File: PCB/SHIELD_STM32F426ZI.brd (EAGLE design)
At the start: 92.4 x 119.5 mm, 16 parts, among them IC1 AS4C16M16SA-6TCN, J1 104239-1430

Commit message: PCB wurde mit kurzer Leitung korrigiert
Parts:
- moved R3 31.7 mm to (65.9, 36.3), turned to 90 degrees
- moved R27 29.6 mm to (62.4, 36.2), turned to 270 degrees
- moved R29 26.7 mm to (64.4, 36.3), turned to 270 degrees
- moved R26 26.0 mm to (59.3, 36.3), turned to 270 degrees
- moved R28 25.8 mm to (57.7, 36.4), turned to 270 degrees
- moved R31 25.5 mm to (56.1, 36.3), turned to 270 degrees
- moved R30 24.8 mm to (60.8, 36.3), turned to 270 degrees
- moved JP3 22.6 mm to (31.6, 82.3), turned to 270 degrees
- moved R1 21.3 mm to (70.0, 36.3)
- moved JP2 20.8 mm to (53.1, 40.3)
- moved C18 19.8 mm to (67.3, 36.3), turned to 270 degrees
- moved R2 17.6 mm to (68.9, 36.4)
- moved J1 11.7 mm to (42.5, 20.3)
- moved JP1 11.2 mm to (39.9, 47.6)
- moved IC1 5.61 mm to (44.1, 79.2)
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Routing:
- net FMC_D0: track 166.7 -> 44.4 mm, vias 0 -> 2
- net FMC_D1: track 160.7 -> 49.7 mm, vias 0 -> 2
- net FMC_SDNE0: track 201.3 -> 91.6 mm, vias 2 -> 1
- net FMC_D4: track 162.8 -> 53.6 mm, vias 2 -> 1
- net FMC_D5: track 163.0 -> 56.3 mm, vias 2 -> 1
- net FMC_D13: track 163.8 -> 65.4 mm, vias 2 -> 0
- net FMC_SDCKE0: track 147.3 -> 53.5 mm, vias 2 -> 3
- net FMC_A5: track 139.1 -> 53.8 mm, vias 2 -> 1
- net FMC_SDNWE: track 122.8 -> 40.0 mm, vias 2 -> 1
- net FMC_A4: track 135.8 -> 53.3 mm, vias 2 -> 0
- net FMC_D6: track 140.1 -> 65.3 mm, vias 2 -> 1
- net FMC_A8: track 108.1 -> 34.1 mm, vias 2 -> 0
- net GND: track 7.15 -> 77.8 mm, vias 5 -> 8
- net FMC_D8: track 98.1 -> 28.5 mm
- net FMC_D7: track 121.8 -> 54.9 mm, vias 2 -> 1
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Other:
- board size 92.4 x 119.5 mm -> 89.8 x 119.7 mm

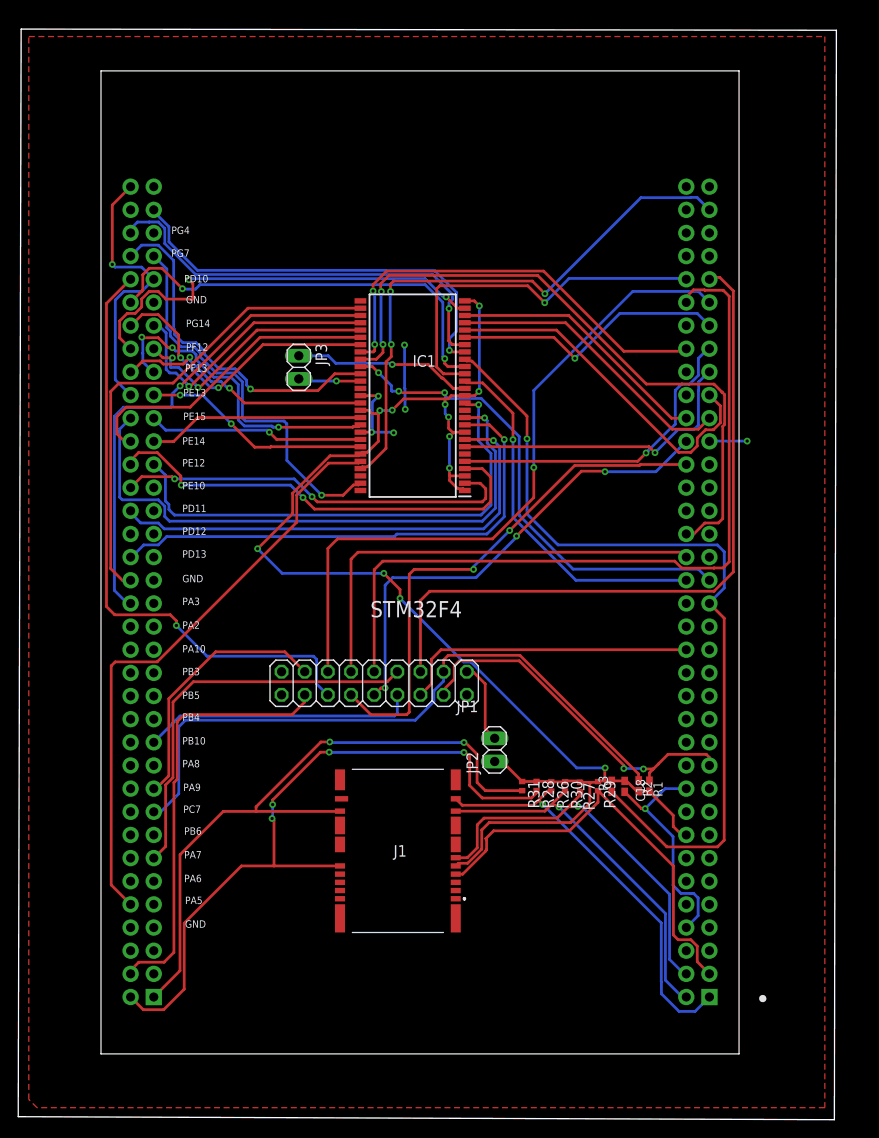
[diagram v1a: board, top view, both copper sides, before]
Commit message: Namen der Elementen und Pin hinzufügen
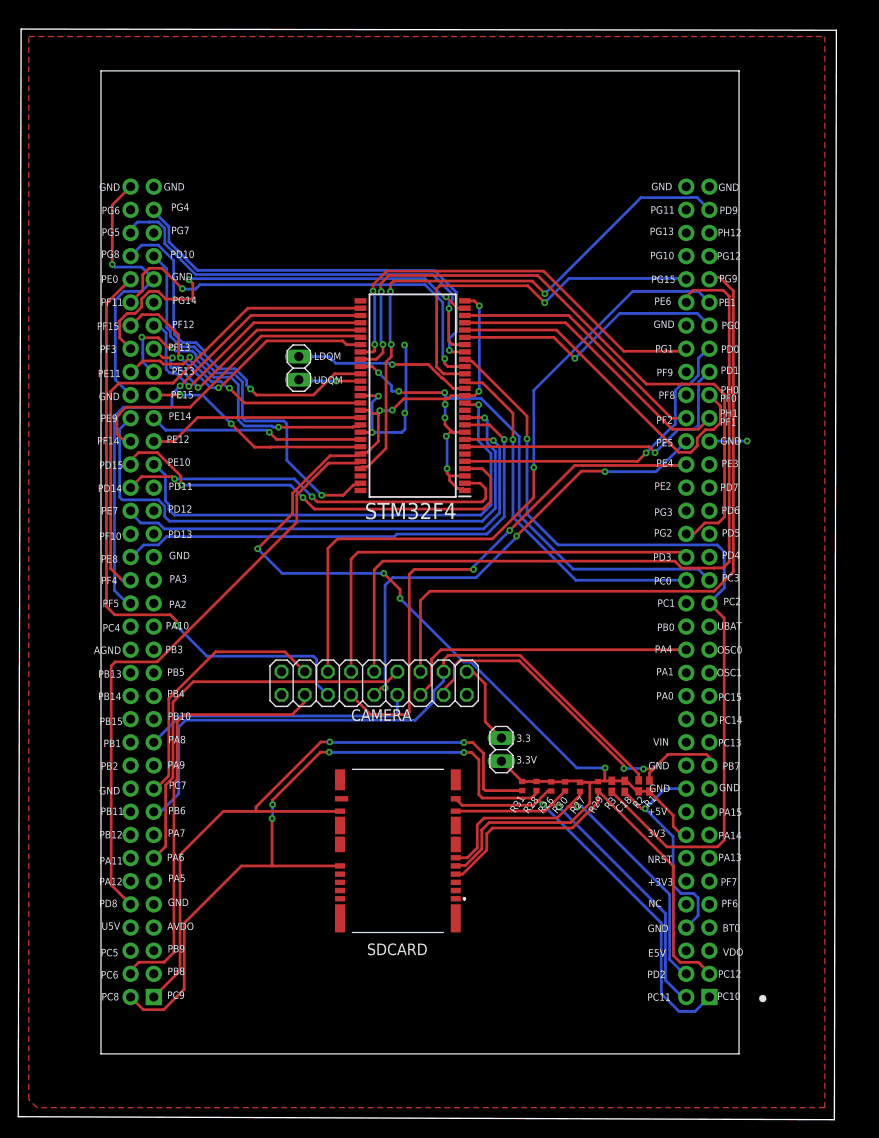
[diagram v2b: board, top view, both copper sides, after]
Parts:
- moved JP2 0.74 mm to (53.8, 40.3)
- moved JP3 0.09 mm to (31.6, 82.2)
- renumbered J1 to SDCARD, JP1 to CAMERA
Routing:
- net GND: track 77.8 -> 80.9 mm, vias 8 -> 7
- net SDIO_CK: track 47.0 -> 47.5 mm
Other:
- board text added: "+3V3"
- board text added: "+5V"
- board text added: "3.3"
- board text added: "3.3V"
- board text added: "3V3"
- board text added: "AGND"
- board text added: "AVDO"
- board text added: "BT0"
- board text added: "E5V"
- board text added: "LDQM"
- board text added: "NC"
- board text added: "NRST"
- board text added: "OSC0"
- board text added: "OSC1"
- board text added: "PA0"
- board text added: "PA1"
- board text added: "PA11"
- board text added: "PA12"
- board text added: "PA13"
- board text added: "PA14"
- board text added: "PA15"
- board text added: "PA4"
- board text added: "PB0"
- board text added: "PB1"
- board text added: "PB11"
- board text added: "PB12"
- board text added: "PB13"
- board text added: "PB14"
- board text added: "PB15"
- board text added: "PB2"
- board text added: "PB7"
- board text added: "PB8"
- board text added: "PB9"
- board text added: "PC0"
- board text added: "PC1"
- board text added: "PC10"
- board text added: "PC11"
- board text added: "PC12"
- board text added: "PC13"
- board text added: "PC14"
- board text added: "PC15"
- board text added: "PC2"
- board text added: "PC3"
- board text added: "PC4"
- board text added: "PC5"
- board text added: "PC6"
- board text added: "PC8"
- board text added: "PC9"
- board text added: "PD0"
- board text added: "PD1"
- board text added: "PD14"
- board text added: "PD15"
- board text added: "PD2"
- board text added: "PD3"
- board text added: "PD4"
- board text added: "PD5"
- board text added: "PD6"
- board text added: "PD7"
- board text added: "PD8"
- board text added: "PD9"
- board text added: "PE0"
- board text added: "PE1"
- board text added: "PE11"
- board text added: "PE2"
- board text added: "PE3"
- board text added: "PE4"
- board text added: "PE5"
- board text added: "PE6"
- board text added: "PE7"
- board text added: "PE8"
- board text added: "PE9"
- board text added: "PF0"
- board text added: "PF1"
- board text added: "PF10"
- board text added: "PF11"
- board text added: "PF14"
- board text added: "PF15"
- board text added: "PF2"
- board text added: "PF3"
- board text added: "PF4"
- board text added: "PF5"
- board text added: "PF6"
- board text added: "PF7"
- board text added: "PF8"
- board text added: "PF9"
- board text added: "PG0"
- board text added: "PG1"
- board text added: "PG10"
- board text added: "PG11"
- board text added: "PG12"
- board text added: "PG13"
- board text added: "PG15"
- board text added: "PG2"
- board text added: "PG3"
- board text added: "PG5"
- board text added: "PG6"
- board text added: "PG8"
- board text added: "PG9"
- board text added: "PH0"
- board text added: "PH1"
- board text added: "PH12"
- board text added: "U5V"
- board text added: "UBAT"
- board text added: "UDQM"
- board text added: "VDO"
- board text added: "VIN"

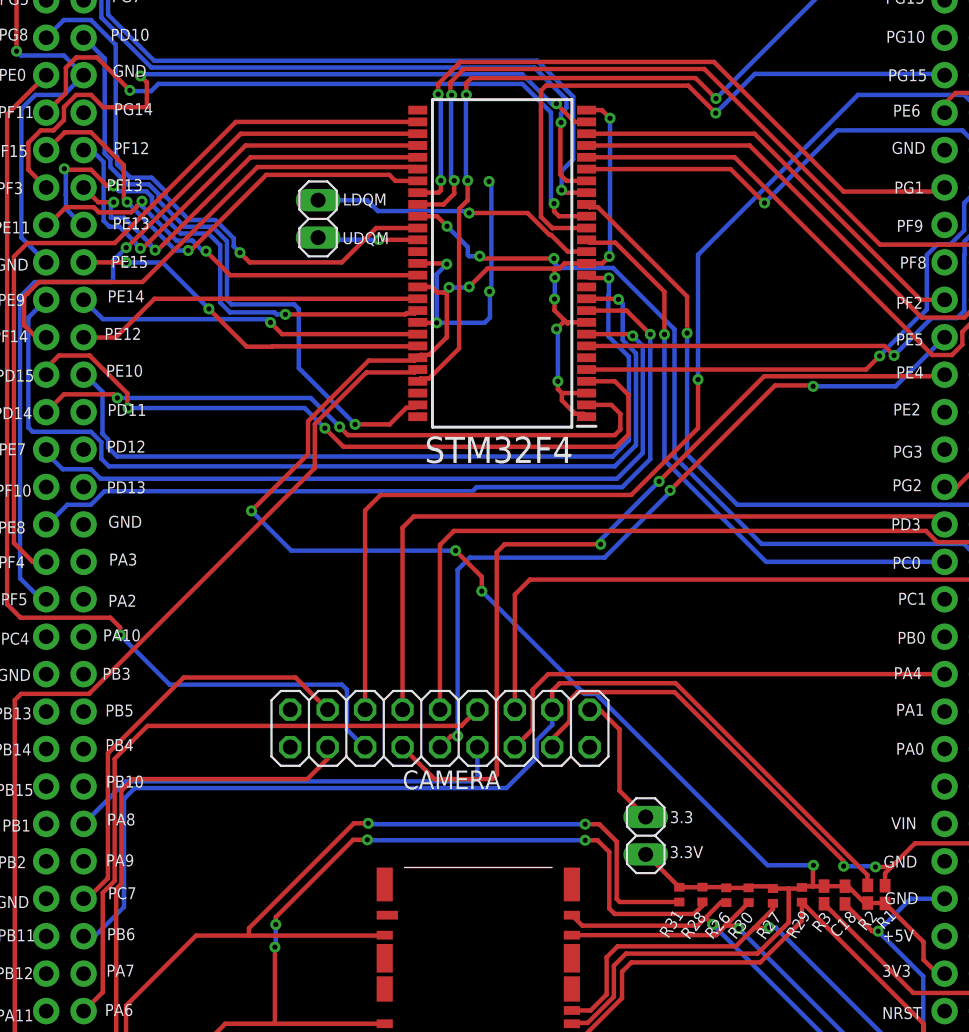
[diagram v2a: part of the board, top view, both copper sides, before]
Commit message: Namen der DCMI-Pins hinzufügen und Position des Kondensators korrigieren
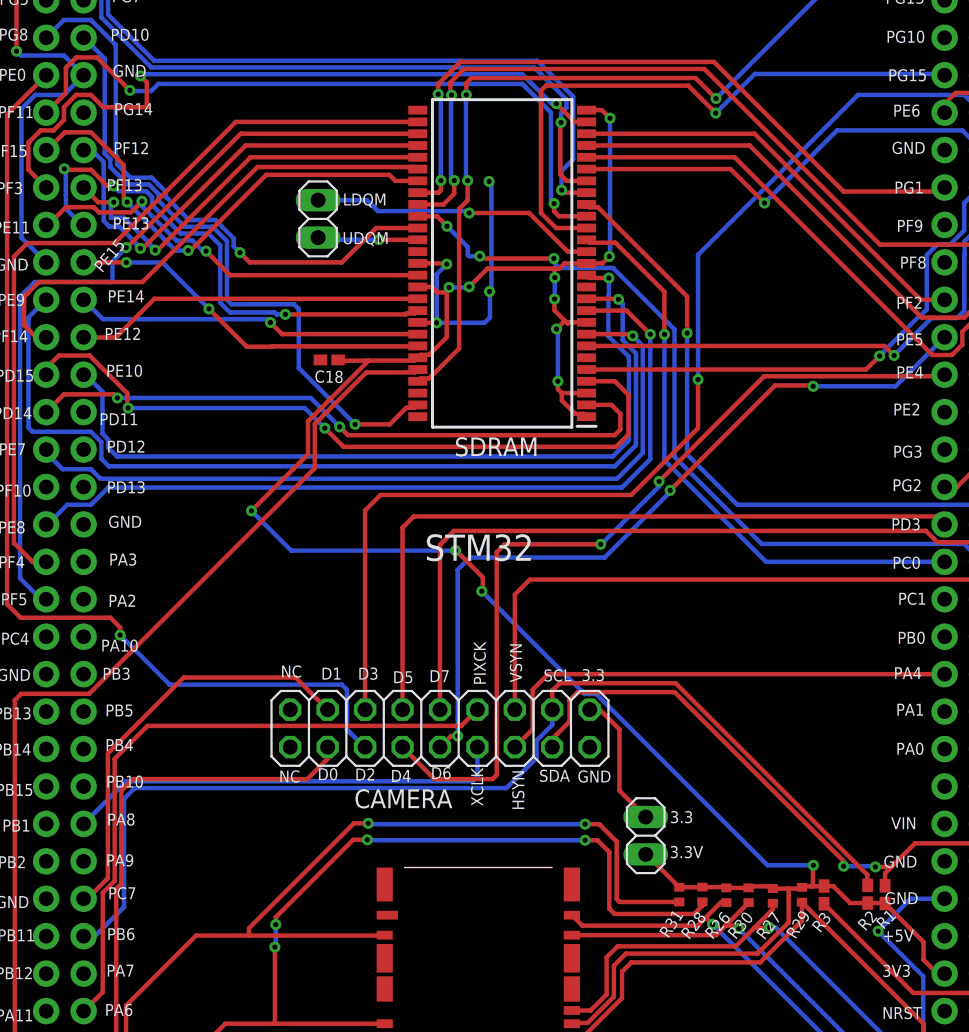
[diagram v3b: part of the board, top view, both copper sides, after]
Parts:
- moved C18 50.4 mm to (32.3, 72.6), turned to 180 degrees
- renumbered IC1 to SDRAM, STM32F4 to STM32
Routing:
- net GND: track 80.9 -> 77.9 mm
- net 3.3V: track 159.2 -> 161.4 mm
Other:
- board text added: "D0"
- board text added: "D1"
- board text added: "D2"
- board text added: "D3"
- board text added: "D4"
- board text added: "D5"
- board text added: "D6"
- board text added: "D7"
- board text added: "HSYN"
- board text added: "PIXCK"
- board text added: "SCL"
- board text added: "SDA"
- board text added: "SDRAM"
- board text added: "VSYN"
- board text added: "XCLK"

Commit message: new update
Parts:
- CAMERA, JP2, JP3: value (none) -> 0
- moved R2 1.25 mm to (67.6, 36.5)
- moved R1 1.13 mm to (68.9, 36.4)
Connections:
- new net PWDN: CAMERA.18, STM32.CN12_29
- net CARD_DET: now also STM32.CN12_11
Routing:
- net CARD_DET: track 0.00 -> 25.3 mm, vias 0 -> 1
- net PWDN: track 0.00 -> 15.0 mm
- net GND: track 77.9 -> 76.7 mm
- net I2C1_SDA: track 40.1 -> 41.2 mm
- net 3.3V: track 161.4 -> 160.8 mm
- net I2C1_SCL: track 72.7 -> 72.2 mm
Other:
- board text added: "AD-HOC"
- board text added: "PA5/CARD_DET"
- board text removed: "PA5"

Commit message: new layout update
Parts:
- renumbered C18 to C1, R26 to R7, R27 to R5, R28 to R8, R29 to R4, R30 to R6, R31 to R9
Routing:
- net FMC_D14: track 62.8 -> 66.6 mm
- net SDIO_D1: track 73.5 -> 75.9 mm
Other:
- board size 89.8 x 119.7 mm -> 83 x 120.2 mm

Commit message: add mosfet and fix GPIOs for sdram and sdcard
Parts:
- removed JP2, JP3: 0, pinhead:1X02
- added Q1: FDN304P, FDN304P:SOT95P237X112-3N
- moved R2 2.20 mm to (69.8, 36.3)
- moved R1 0.99 mm to (67.9, 36.3)
- moved R3 0.49 mm to (66.4, 36.3), turned to 270 degrees
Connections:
- removed net FMC_SDCKE0: SDRAM.37, STM32.CN11_37
- removed net FMC_SDNE0: R3.1, SDRAM.19, STM32.CN11_35
- removed net I2C1_SCL: CAMERA.3, R2.1, STM32.CN12_17
- removed net I2C1_SDA: CAMERA.4, R1.1, STM32.CN11_21
- new net FMC_SDCKE1: SDRAM.37, STM32.CN12_29
- new net FMC_SDNE1: R3.1, SDRAM.19, STM32.CN12_17
- new net GATE: Q1.1, STM32.CN11_35
- new net I2C2_SCL: CAMERA.3, R2.1, STM32.CN12_25
- new net I2C2_SDA: CAMERA.4, R1.1, STM32.CN12_18
- new net RESET: CAMERA.17, STM32.CN12_31
- net 3.3: now also Q1.3; no longer JP2.2
- net 3.3V: now also Q1.2; no longer JP2.1
- net DCMI_D2: now also STM32.CN11_66; no longer STM32.CN12_64
- net DCMI_D3: now also STM32.CN11_70; no longer STM32.CN11_61
- net DCMI_VSYNC: now also STM32.CN11_21; no longer STM32.CN11_63
- net LDQM: now also STM32.CN12_64; no longer JP3.1
- net PWDN: now also STM32.CN12_27; no longer STM32.CN12_29
- net UDQM: now also STM32.CN11_61; no longer JP3.2
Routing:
- net FMC_SDNE1: track 0.00 -> 110.5 mm, vias 0 -> 5
- net FMC_SDNE0: track 91.6 -> 0.00 mm, vias 1 -> 0
- net I2C2_SCL: track 0.00 -> 77.7 mm
- net I2C1_SCL: track 72.2 -> 0.00 mm
- net I2C2_SDA: track 0.00 -> 68.5 mm
- net GND: track 76.7 -> 20.5 mm, vias 7 -> 4
- net FMC_SDCKE0: track 53.5 -> 0.00 mm, vias 3 -> 0
- net LDQM: track 19.7 -> 72.6 mm
- net UDQM: track 6.82 -> 55.8 mm, vias 1 -> 2
- net FMC_SDCKE1: track 0.00 -> 46.2 mm, vias 0 -> 2
- net I2C1_SDA: track 41.2 -> 0.00 mm, vias 2 -> 0
- net DCMI_VSYNC: track 77.6 -> 47.3 mm
- net GATE: track 0.00 -> 22.4 mm, vias 0 -> 1
- net RESET: track 0.00 -> 16.3 mm
- net 3.3: track 9.25 -> 18.0 mm
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- added copper zone on layer 16, net GND
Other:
- board text added: "PWDN"
- board text removed: "LDQM"
- board text removed: "UDQM"
